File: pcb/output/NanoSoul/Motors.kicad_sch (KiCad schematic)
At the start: 15 parts

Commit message: pcb: 3mm 白边 + J2/J7 离 J4 + DRC 丝印告警清零
- 最外围 3mm 白边：板放大到 94×92（Ø108 切边收小到 7/8mm），铜/器件焊盘距最外缘 ≥3mm
  （自动布线内缩 3mm；顶排 J5/J6 下移、J8 左移退出白边区）。
- J2/J7 离 J4：右月牙整体右移 1.6mm，离 J4 本体 +0.83mm（原相擦 0.78mm）。
- DRC = 0 warning：5 个位号(D4/D5/Q1/U1/U7)挪开、接线图例升到 0.8mm 并缩短、
  删 J3/J4 压挖孔丝印、隐藏 6 安装孔与 U7 位号。
- 17.8mm 母座行距核对通过；4 个 M3 安装孔成规则 54×82 矩形（旧版钉在 Ø108 圆外、钻不出，已修正）。
- 余 MOT_RTN/GND 各 1 段跨挖孔大电流网/地：按 docs 铁律出板前人工绕挖孔补（GND 建议铺地铜），
  网表连接关系正确（其余 170 网 0 短路）。原理图 ERC 不适用：circuit-synth 开源导出无导线、
  网表为真值源。详见 docs/05 §9.1。
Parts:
- C10, C11, C12, C13, J5, J6, J7, R10, R11, R12, R13, R14, R9, U4, U5: hierarchy_path /8a83f0c7-8320-4874-8ea1-ef8ee28a330a/81dd35de-56dd-43b6-a5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 -> /cc6d016d-315a-4023-b551-816edf85e992/b5003982-3f4a-4b33-96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; root_uuid 8a83f0c7-8320-4874-8ea1-ef8ee28a330a -> cc6d016d-315a-4023-b551-816edf85e992

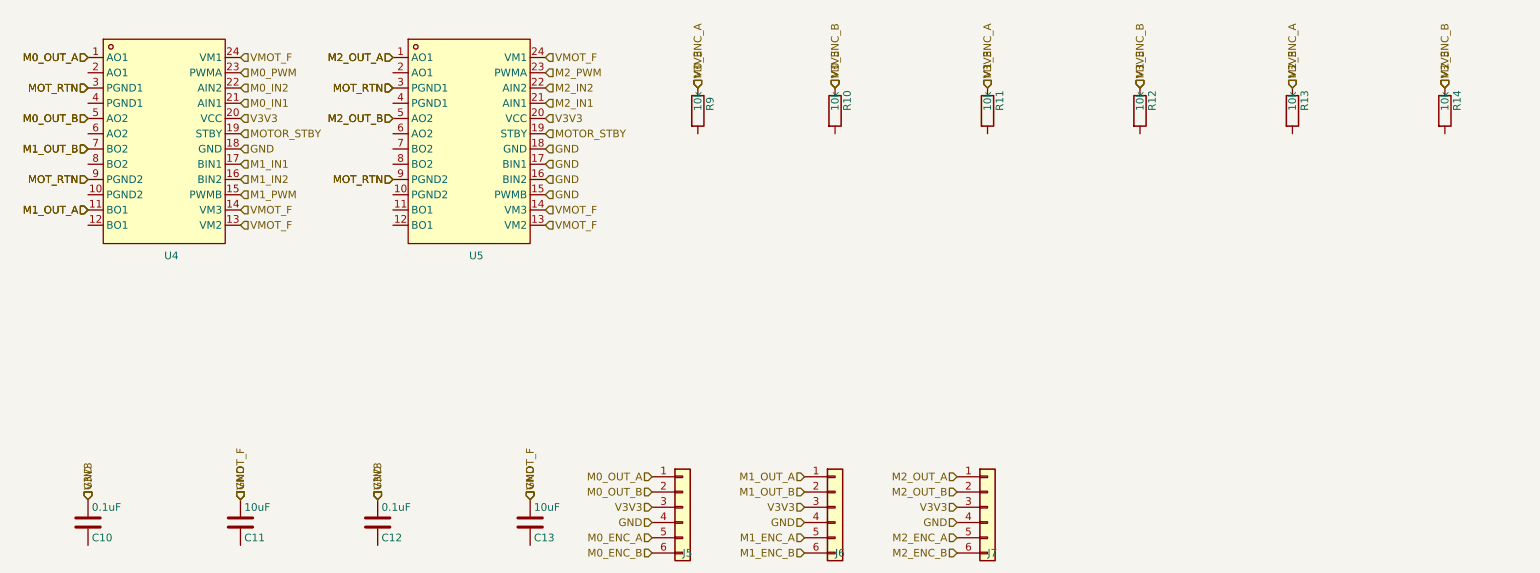
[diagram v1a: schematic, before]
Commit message: pcb: schematic-parity 真零(零 ignore) + 重导 Gerber
DRC `--schematic-parity --severity-all` = 0 violation / 0 unconnected /
0 schematic-parity,62 项检查全置 error、零 ignore(旧版的 7 项 ignore 全部真修掉,
非关检查)。verify_board 65/65、布线 778 走线+60 过孔未动。

- 修通 circuit-synth 原理图连通性:它把一器件所有网名标签堆在 pin1 → KiCad 推断错网。
  按 .net 逐脚在真实连接点重放 global_label(fix_sch_labels),net_conflict 199→0;
  真 NC 脚在板上配同名 unconnected- 网对齐(assign_nc_nets)。
- 板 Value 回填真实值(顺修「板上 Value=封装名」的 BOM bug)、lib_id 去库前缀(fix_board_meta);
  原理图删 circuit-synth 私有字段/封装过滤器、补缺失 Value(fix_sch_fields);
  J2 attr→through_hole(USB-C 靠屏蔽脚 THT 安装,属实);4×M3 孔标 board_only。
- 唯一保留例外 = J2(USB-C)连接器内部 DRU(实测 0.10mm 铜/0.185mm 孔,JLC 可造;
  KiCad 官方 USB_C_Receptacle_HRO 封装内部孔距也仅 0.15mm → 换封装消不掉、
  改窄焊盘会伤实焊。限 J2 内部两两对象,不放宽对板上走线)。
- 重导 Gerber(9 层 Protel 扩展名 + Excellon 钻孔)+ BOM/CPL。
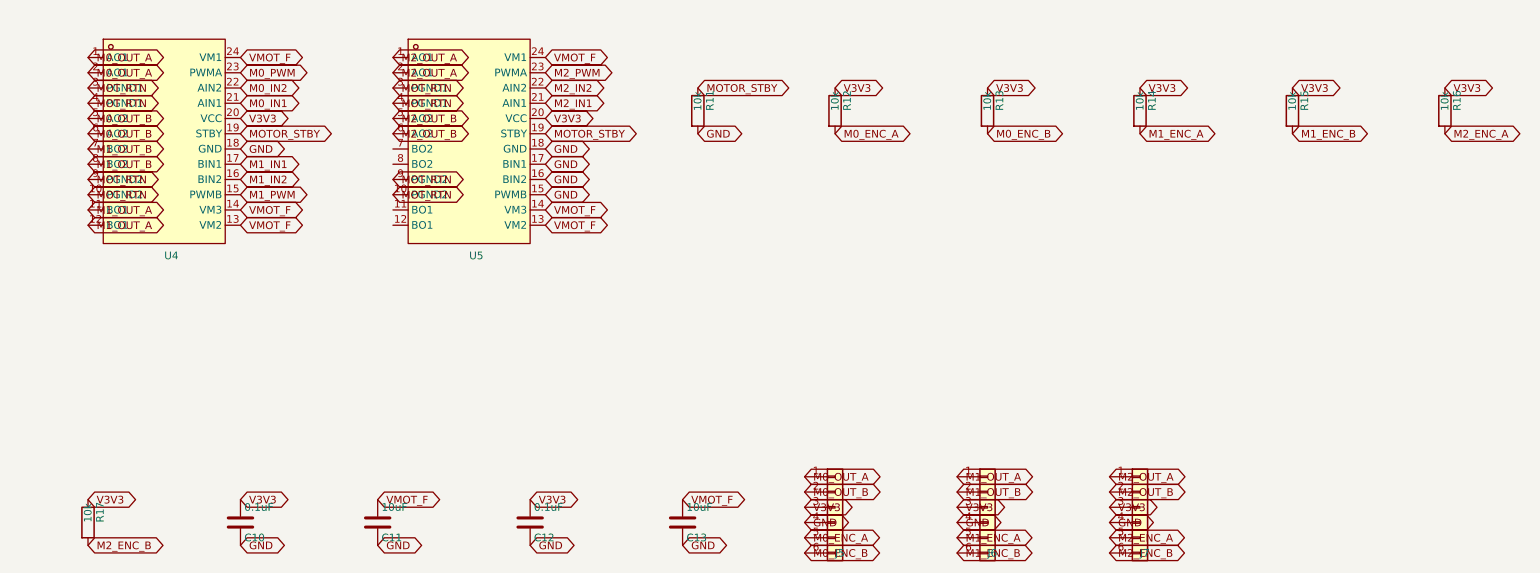
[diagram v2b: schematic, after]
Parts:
- removed R10, R9: 10k, Resistor_SMD:R_0603_1608Metric, symbol Device:R
- added R15, R16, R17: 10k, R_0603_1608Metric, symbol Device:R
- C10, C12: footprint Capacitor_SMD:C_0603_1608Metric -> C_0603_1608Metric; hierarchy_path /cc6d016d-315a-4023-b551-816edf85e992/b5003982-3f4a-4b33-96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 -> (none); project_name NanoSoul -> (none); root_uuid cc6d016d-315a-4023-b551-816edf85e992 -> (none)
- C11, C13: footprint Capacitor_SMD:C_0805_2012Metric -> C_0805_2012Metric; hierarchy_path /cc6d016d-315a-4023-b551-816edf85e992/b5003982-3f4a-4b33-96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 -> (none); project_name NanoSoul -> (none); root_uuid cc6d016d-315a-4023-b551-816edf85e992 -> (none)
- J5, J6, J7: value (none) -> PinHeader_1x06_P2.54mm_Vertical; footprint Connector_PinHeader_2.54mm:PinHeader_1x06_P2.54mm_Vertical -> PinHeader_1x06_P2.54mm_Vertical; hierarchy_path /cc6d016d-315a-4023-b551-816edf85e992/b5003982-3f4a-4b33-96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 -> (none); project_name NanoSoul -> (none); root_uuid cc6d016d-315a-4023-b551-816edf85e992 -> (none)
- R11, R12, R13, R14: footprint Resistor_SMD:R_0603_1608Metric -> R_0603_1608Metric; hierarchy_path /cc6d016d-315a-4023-b551-816edf85e992/b5003982-3f4a-4b33-96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 -> (none); project_name NanoSoul -> (none); root_uuid cc6d016d-315a-4023-b551-816edf85e992 -> (none)
- U4, U5: value (none) -> SSOP-24_L8.3-W5.6-P0.65-LS7.6-BL; footprint nanosoul:SSOP-24_L8.3-W5.6-P0.65-LS7.6-BL -> SSOP-24_L8.3-W5.6-P0.65-LS7.6-BL; hierarchy_path /cc6d016d-315a-4023-b551-816edf85e992/b5003982-3f4a-4b33-96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 -> (none); project_name NanoSoul -> (none); root_uuid cc6d016d-315a-4023-b551-816edf85e992 -> (none)
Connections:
- net GND: now also C10.2, C11.2, C12.2, C13.2, R11.2; no longer C10.1, C11.1, C12.1, C13.1, J5.3 (Pin_3), J5.5 (Pin_5), J5.6 (Pin_6), J6.3 (Pin_3), J6.5 (Pin_5), J6.6 (Pin_6), J7.3 (Pin_3), J7.5 (Pin_5), J7.6 (Pin_6), R11.1, R12.1, R13.1, R14.1, U4.13 (VM2), U4.14 (VM3), U4.20 (VCC), U4.24 (VM1), U5.13 (VM2), U5.14 (VM3), U5.20 (VCC), U5.24 (VM1)
- net M0_OUT_A: now also U4.2 (AO1)
- net M0_OUT_B: now also U4.6 (AO2)
- net M1_OUT_A: now also U4.12 (BO1)
- net M1_OUT_B: now also U4.8 (BO2)
- net M2_OUT_A: now also U5.2 (AO1)
- net M2_OUT_B: now also U5.6 (AO2)
- net MOTOR_STBY: now also R11.1
- net MOT_RTN: now also U4.10 (PGND2), U4.4 (PGND1), U5.10 (PGND2), U5.4 (PGND1)
- net M0_ENC_B: now reaches R13.2
- net M0_ENC_B: now also J5.6 (Pin_6)
- net M1_ENC_A: now reaches R14.2
- net M1_ENC_A: now also J6.5 (Pin_5)
- net M0_ENC_A: now reaches R12.2
- net M0_ENC_A: now also J5.5 (Pin_5)
- new net M1_ENC_B: J6.6 (Pin_6), R15.2
- new net M2_ENC_A: J7.5 (Pin_5), R16.2
- new net M2_ENC_B: J7.6 (Pin_6), R17.2
- new net V3V3: C10.1, C12.1, J5.3 (Pin_3), J6.3 (Pin_3), J7.3 (Pin_3), R12.1, R13.1, R14.1, R15.1, R16.1, R17.1, U4.20 (VCC), U5.20 (VCC)
- new net VMOT_F: C11.1, C13.1, U4.13 (VM2), U4.14 (VM3), U4.24 (VM1), U5.13 (VM2), U5.14 (VM3), U5.24 (VM1)
